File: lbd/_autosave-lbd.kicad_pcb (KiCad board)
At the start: 2 copper layers, 113.1 x 94.6 mm, 42 parts

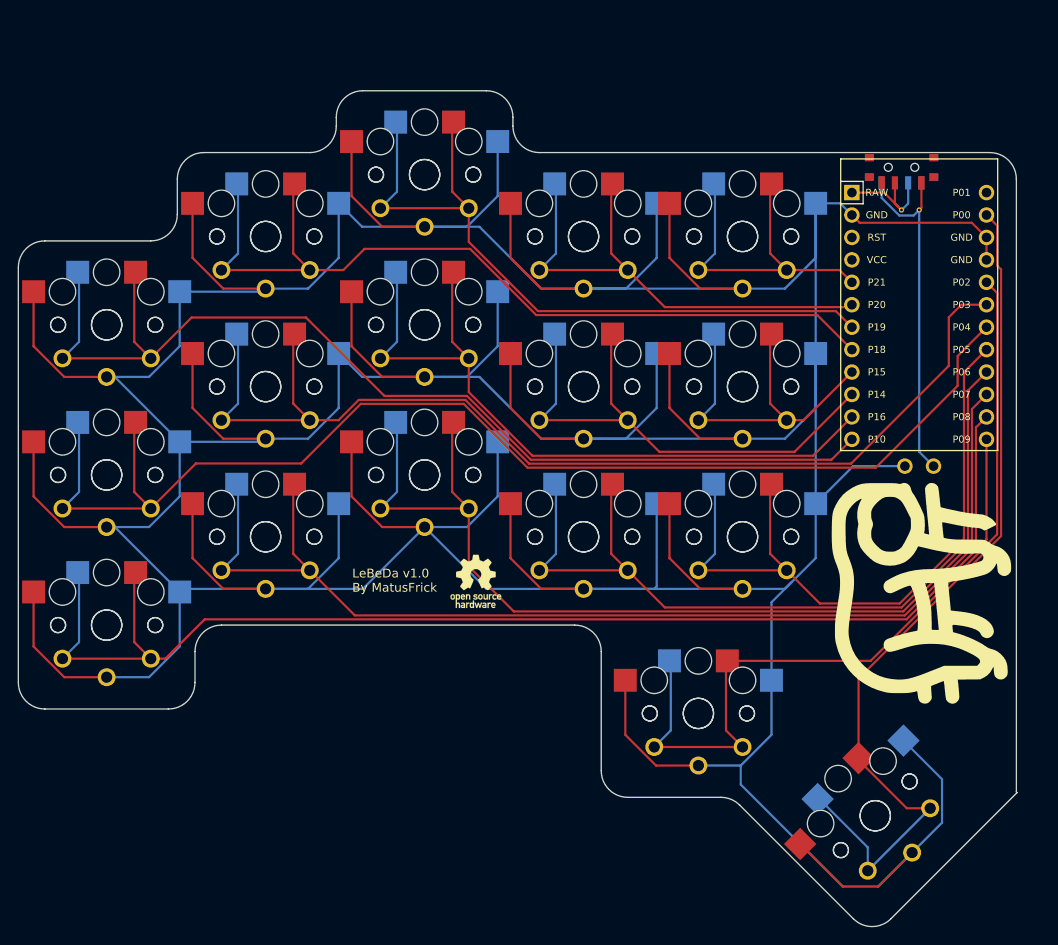
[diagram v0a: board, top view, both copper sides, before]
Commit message: Routed with silk screen
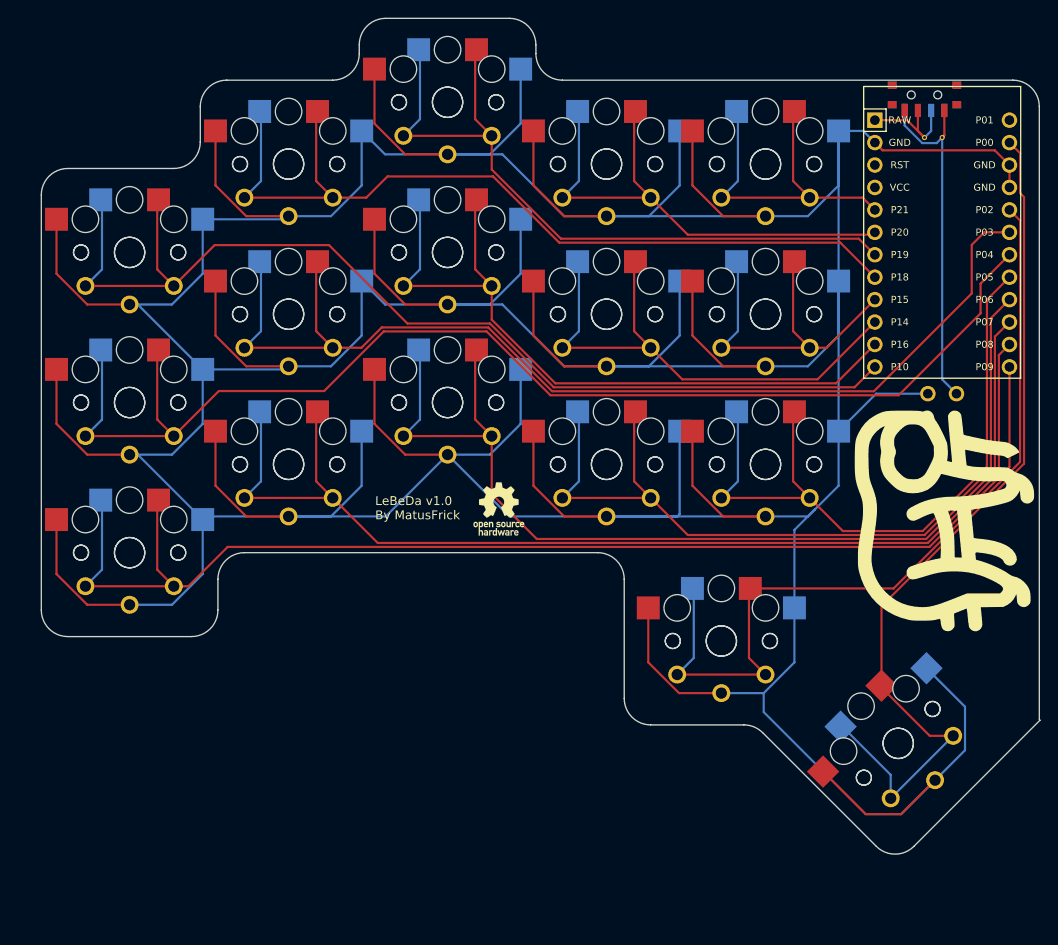
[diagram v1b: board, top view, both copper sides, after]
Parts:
- moved ? 8.60 mm to (194.4, 52.1)
- moved G*** 8.60 mm to (196.7, 100.0) (x2)
- moved REF** 8.60 mm to (146.2, 98.7)
- moved S17 8.60 mm to (140.4, 52.6)
- moved S18 8.60 mm to (140.4, 52.6)
- moved S33 8.60 mm to (191.5, 125.2)
- moved S34 8.60 mm to (191.5, 125.2)
- moved S11 8.60 mm to (122.5, 59.6)
- moved S12 8.60 mm to (122.5, 59.6)
- moved REF** 8.60 mm to (194.4, 56.6)
- moved REF** 8.60 mm to (196.4, 56.6)
- moved S23 8.60 mm to (158.4, 59.6)
- moved S24 8.60 mm to (158.4, 59.6)
- moved S29 8.60 mm to (176.4, 59.6)
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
